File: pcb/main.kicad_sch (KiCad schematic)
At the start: 3 parts, among them J6 SJ2-25773B-SMT-TR, U7 450405020524

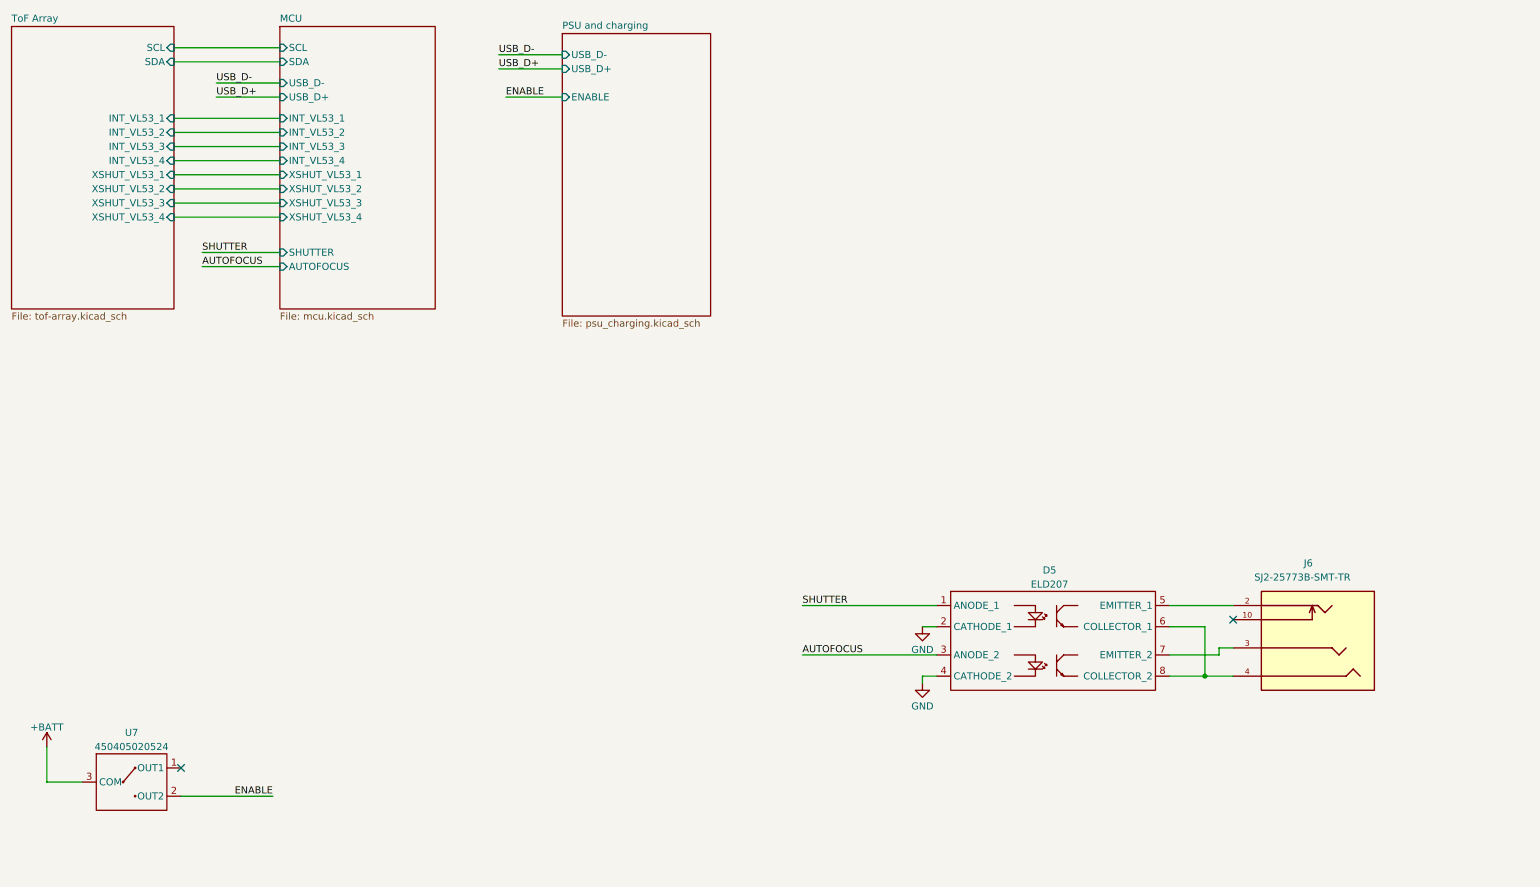
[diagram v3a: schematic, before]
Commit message: refactored components and layout
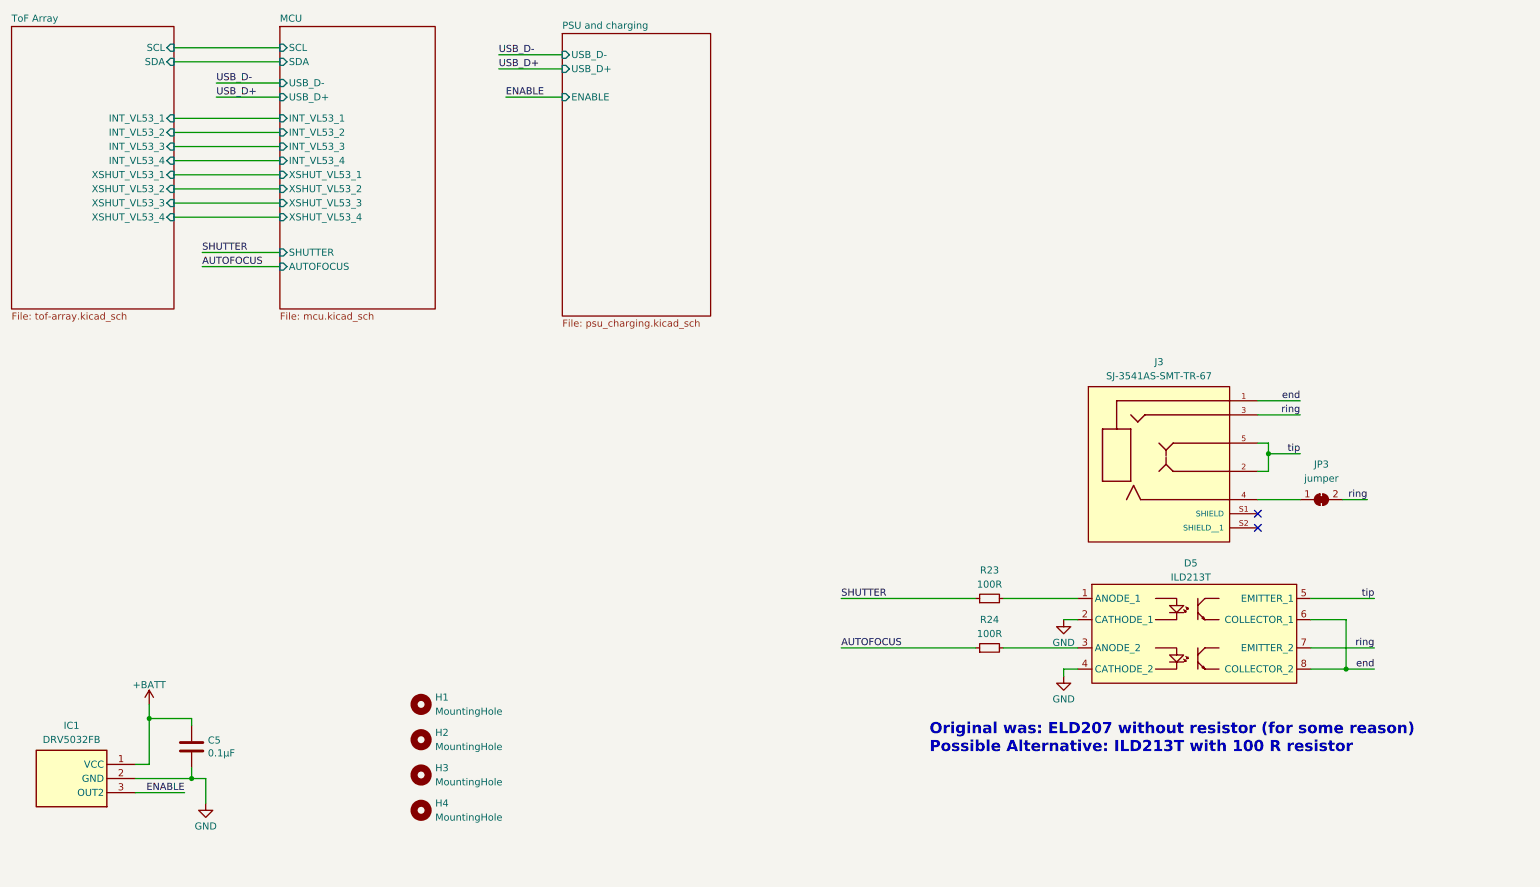
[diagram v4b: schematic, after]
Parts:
- removed J6: SJ2-25773B-SMT-TR, SJ-25773B-SMT:CUI_SJ2-25773B-SMT-TR, symbol SJ2-25773B-SMT-TR:SJ2-25773B-SMT-TR
- removed U7: 450405020524, 450405020524:450405020524, symbol 450405020524:450405020524
- added C5: 0.1µF, Capacitor_SMD:C_0603_1608Metric, symbol Device:C
- added H1, H2, H3, H4: MountingHole, MountingHole:MountingHole_2.5mm_Pad_Via, symbol Mechanical:MountingHole
- added IC1: DRV5032FB, DRV5032DULPGM:DRV5032DULPGM, symbol DRV5032DULPGM:DRV5032DULPGM
- added J3: SJ-3541AS-SMT-TR-67, SJ-3541AS-SMT-TR-67:CUI_SJ-3541AS-SMT-TR-67, symbol SJ-3541AS-SMT-TR-67:SJ-3541AS-SMT-TR-67
- added JP3: jumper, Jumper:SolderJumper-2_P1.3mm_Bridged_RoundedPad1.0x1.5mm, symbol Jumper:SolderJumper_2_Bridged
- added R23, R24: 100R, Resistor_SMD:R_0603_1608Metric, symbol Device:R_Small
- D5: value ELD207 -> ILD213T
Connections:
- net +BATT: now also C5.1, IC1.1 (VCC)
- net AUTOFOCUS: now also R24.1; no longer D5.3 (ANODE_2)
- net ENABLE: now also IC1.3 (OUT2)
- net GND: now also C5.2, IC1.2 (GND)
- net SHUTTER: now also R23.1; no longer D5.1 (ANODE_1)
- net tip: now reaches D5.5 (EMITTER_1)
- net tip: now also J3.2, J3.5
- net end: now reaches D5.6 (COLLECTOR_1), D5.8 (COLLECTOR_2)
- net end: now also J3.1
- net ring: now reaches D5.7 (EMITTER_2)
- net ring: now also J3.3, JP3.2 (B)
- new net: D5.1 (ANODE_1), R23.2
- new net: D5.3 (ANODE_2), R24.2
- new net: J3.4, JP3.1 (A)
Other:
- note added: "Original was: ELD207 without resistor (for some reason) Possible Alternative: ILD213T with 100 R resistor"

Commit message: re-organise components + added housing data
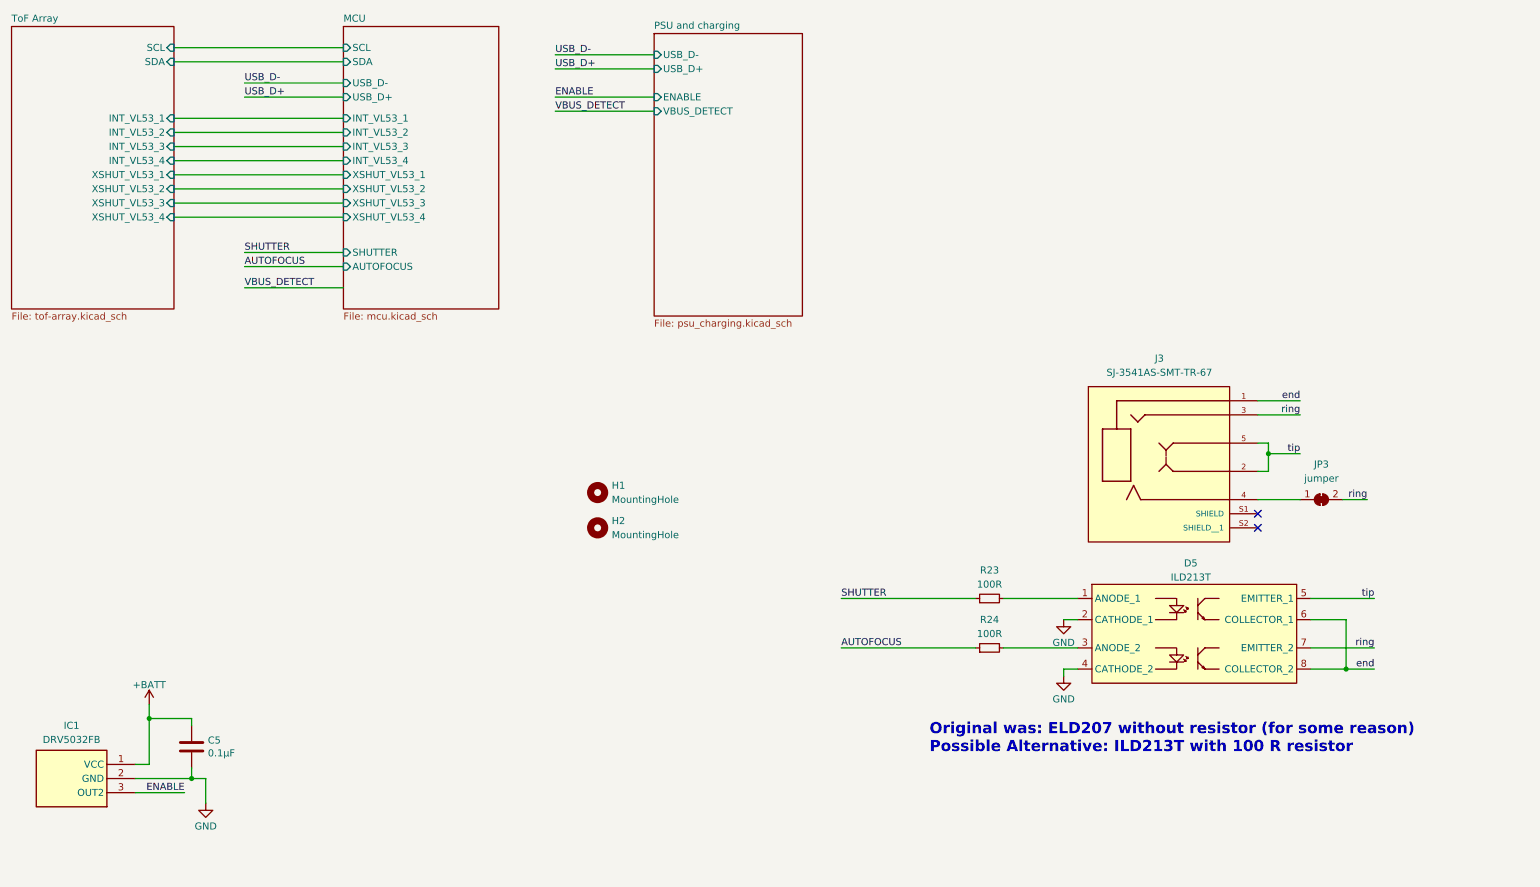
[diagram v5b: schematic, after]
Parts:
- removed H3, H4: MountingHole, MountingHole:MountingHole_2.5mm_Pad_Via, symbol Mechanical:MountingHole
- H1, H2: footprint MountingHole:MountingHole_2.5mm_Pad_Via -> MountingHole:MountingHole_2.5mm_Pad
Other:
- sheet PSU and charging ports: added VBUS_DETECT; removed none
- moved on the sheet: H1, H2

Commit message: Replaced RP2040 with ESP32 + Schematics + Layouting
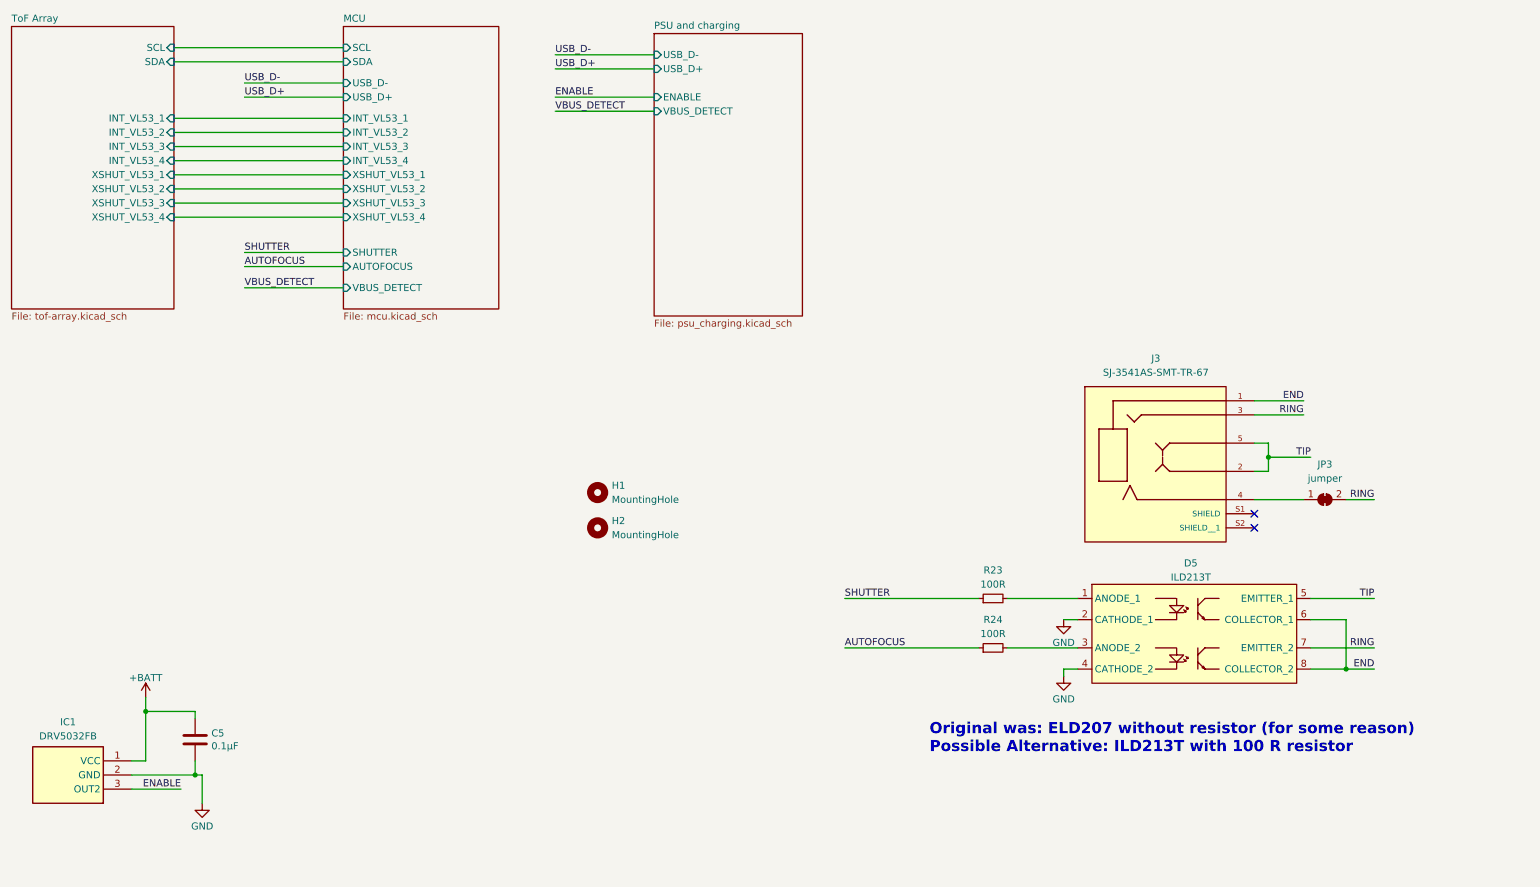
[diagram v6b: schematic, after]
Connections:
- net end renamed END
- net ring renamed RING
- net tip renamed TIP
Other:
- sheet MCU ports: added VBUS_DETECT; removed none
- moved on the sheet: C5, IC1, J3, JP3, R23, R24
